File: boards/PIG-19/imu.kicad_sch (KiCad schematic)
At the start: 4 parts

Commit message: V1 of PCB
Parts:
- added RH_L1: Conn_01x09_Pin, Connector_PinHeader_2.54mm:PinHeader_1x09_P2.54mm_Vertical, symbol Connector:Conn_01x09_Pin
- added RH_S1: Conn_01x05_Pin, Connector_PinHeader_2.54mm:PinHeader_1x05_P2.54mm_Vertical, symbol Connector:Conn_01x05_Pin
- C8: footprint Capacitor_SMD:C_0805_2012Metric -> Capacitor_SMD:C_0603_1608Metric
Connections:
- net +3V3: now also RH_L1.1 (Pin_1)
- net GND: now also RH_L1.3 (Pin_3), RH_S1.5 (Pin_5)
- net SCL: now also RH_L1.5 (Pin_5)
- net SDA: now also RH_L1.4 (Pin_4)
- no-connect marks 2 -> 11

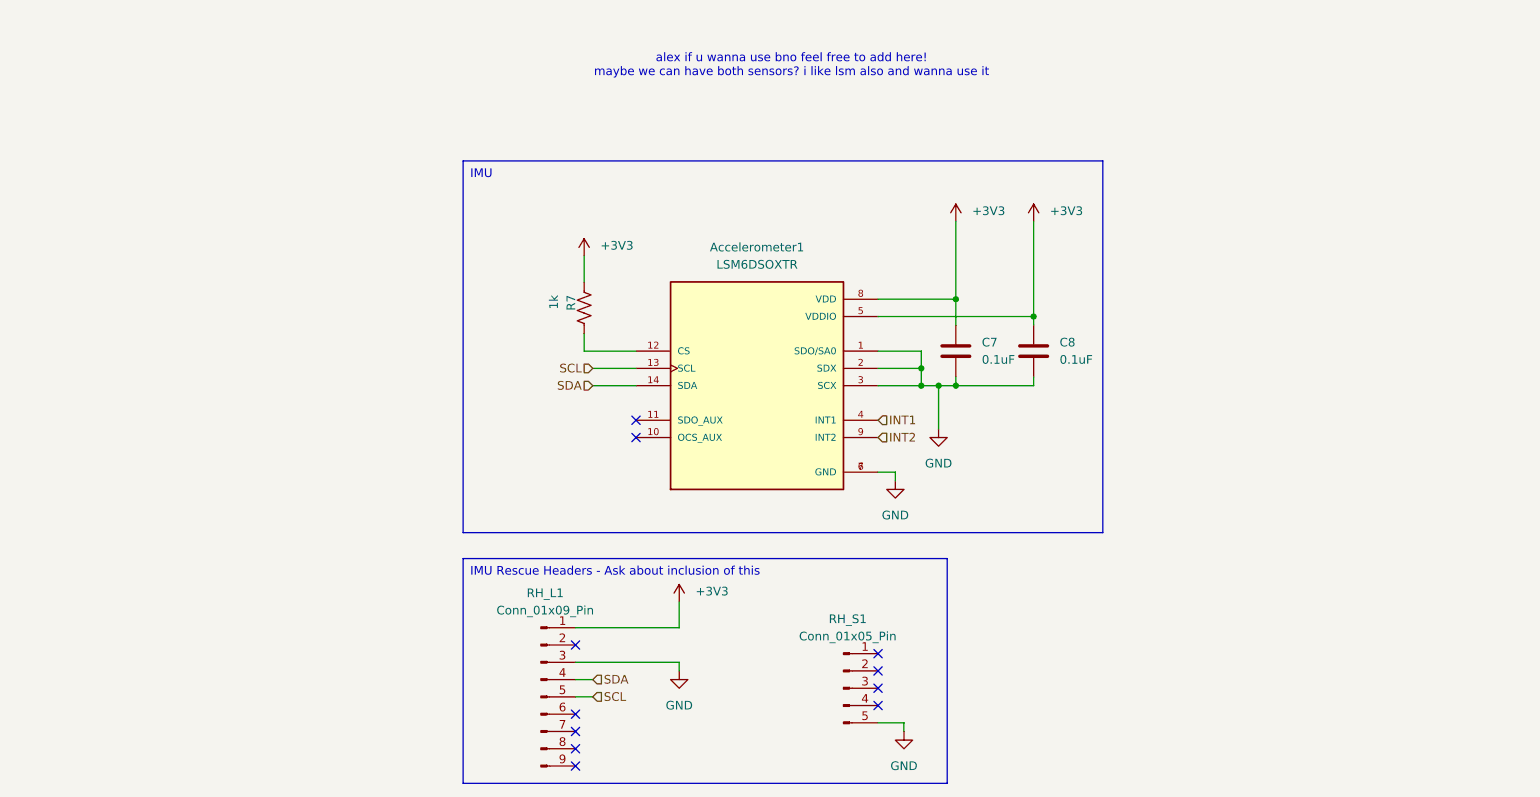
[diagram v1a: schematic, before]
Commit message: I2C pull up resistors
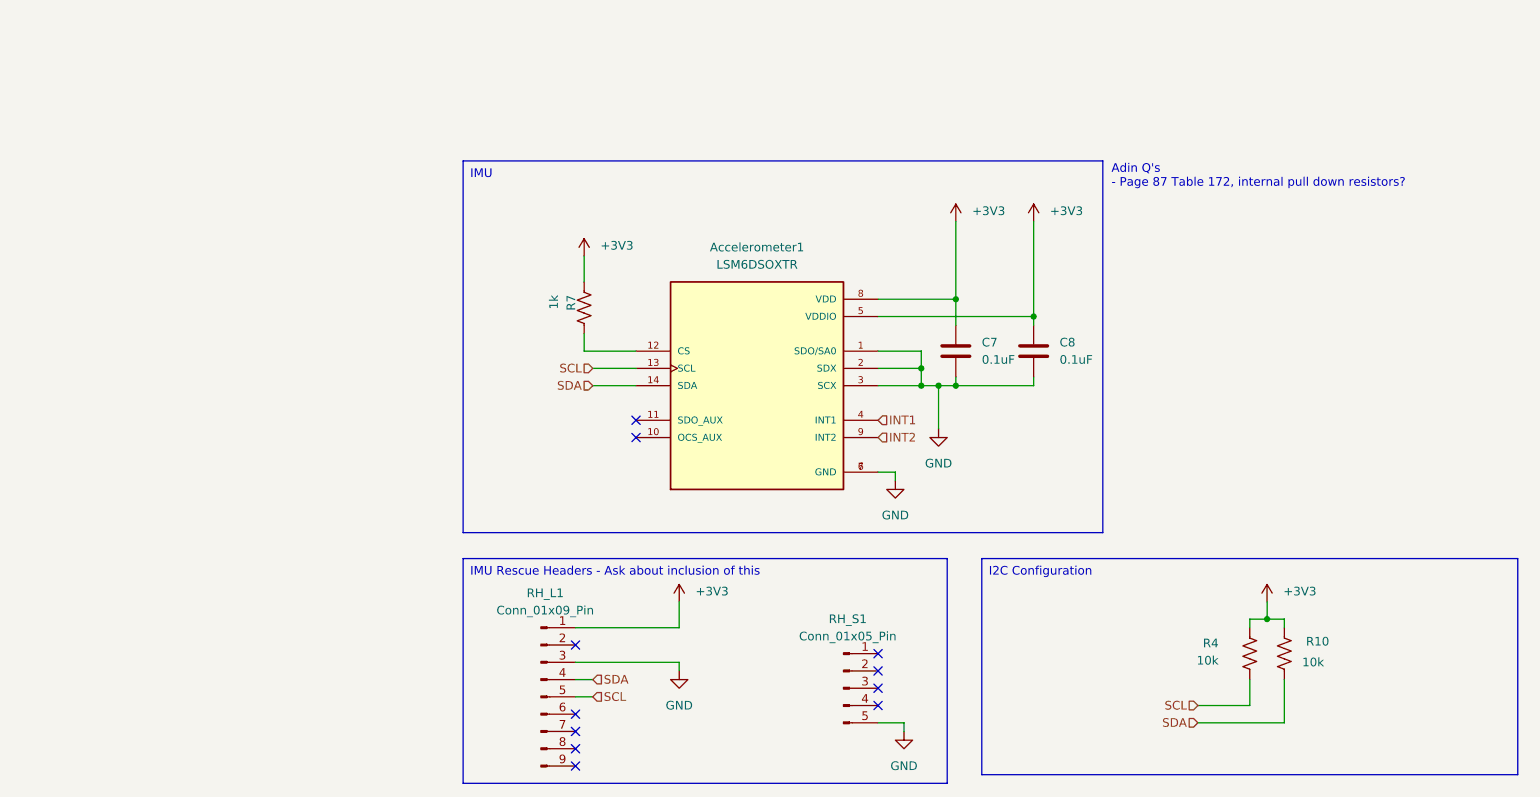
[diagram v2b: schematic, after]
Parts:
- added R10, R4: 10k, Resistor_SMD:R_0603_1608Metric, symbol Device:R_US
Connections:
- net +3V3: now also R10.2, R4.2
- net SCL: now also R4.1
- net SDA: now also R10.1
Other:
- note added: "Adin Q's - Page 87 Table 172, internal pull down resistors?"
- note removed: "alex if u wanna use bno feel free to add here! maybe we can have both sensors? i like lsm also and wanna use it"

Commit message: commit for adin to review
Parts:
- removed RH_L1: Conn_01x09_Pin, Connector_PinHeader_2.54mm:PinHeader_1x09_P2.54mm_Vertical, symbol Connector:Conn_01x09_Pin
- C7: footprint Capacitor_SMD:C_0805_2012Metric -> Capacitor_SMD:C_0603_1608Metric
- R7: footprint Resistor_SMD:R_0805_2012Metric -> Resistor_SMD:R_0603_1608Metric
- renumbered RH_S1 to BNO1
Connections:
- net +3V3: now also BNO1.2 (Pin_2)
- net GND: now also BNO1.4 (Pin_4); no longer BNO1.5 (Pin_5)
- net SCL: now also BNO1.5 (Pin_5)
- net SDA: now also BNO1.1 (Pin_1)
- net INT3: now reaches BNO1.3 (Pin_3)
- no-connect marks 11 -> 2
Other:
- note added: "Adin Q's - Page 87 Table 172, internal pull down resistors on interrupt pins?"
- note removed: "Adin Q's - Page 87 Table 172, internal pull down resistors?"
- moved on the sheet: Accelerometer1, BNO1, C7, C8, R10, R4, R7

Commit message: board updates
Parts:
- BNO1: now left out of the parts list
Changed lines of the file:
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@@
 		(unit 1)
 		(exclude_from_sim no)
-		(in_bom yes)
+		(in_bom no)
 		(on_board yes)
 		(dnp no)

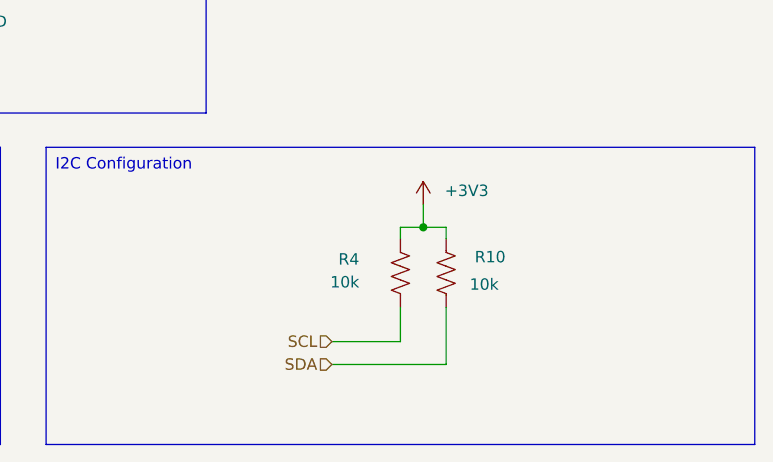
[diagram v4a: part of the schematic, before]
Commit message: Added BOM for main board
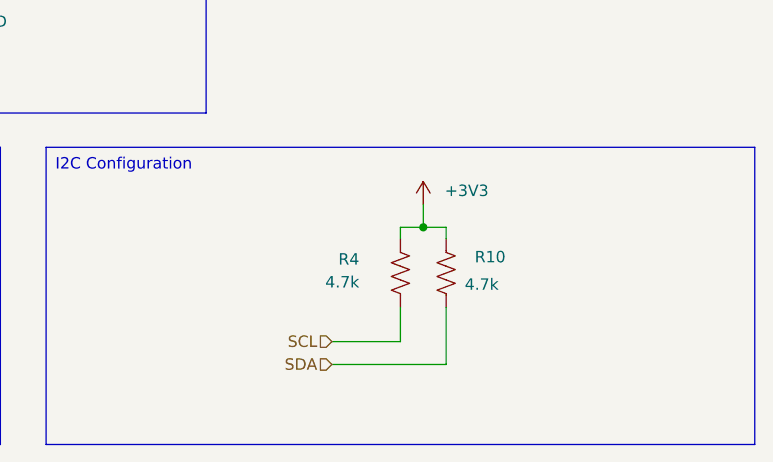
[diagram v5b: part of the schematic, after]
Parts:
- R10, R4: value 10k -> 4.7k
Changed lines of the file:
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@@
 			)
 		)
-		(property "Value" "10k"
+		(property "Value" "4.7k"
 			(at 145.288 130.556 0)
 			(effects
@@
 			)
 		)
-		(property "Value" "10k"
+		(property "Value" "4.7k"
 			(at 160.782 130.81 0)
 			(effects
